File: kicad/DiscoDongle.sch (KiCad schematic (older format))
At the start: 21 parts, among them J1 USB_B, J2 RJ45, U1 FT232RL, U2 ISL81487E

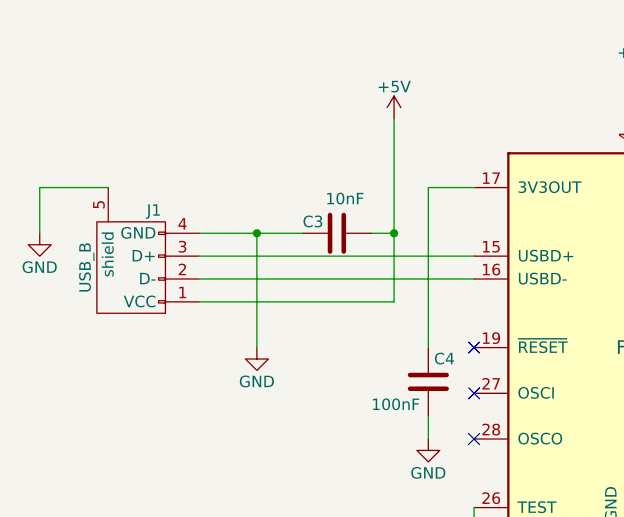
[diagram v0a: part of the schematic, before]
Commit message: Change USB to micro-B. Add part numbers
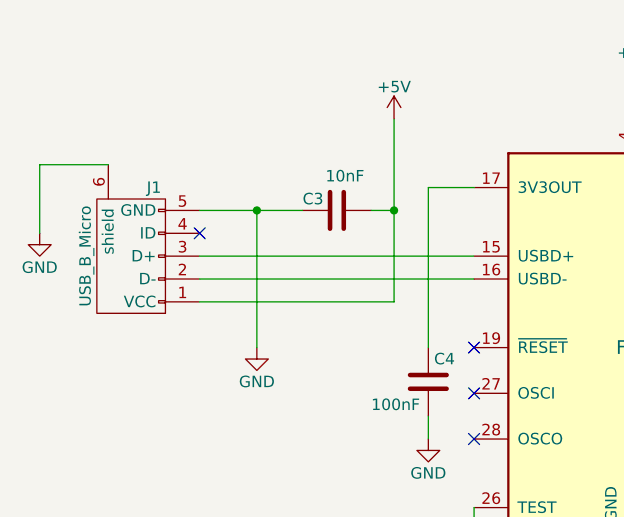
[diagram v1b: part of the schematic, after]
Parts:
- removed J1: USB_B, Connect:USB_B, symbol USB_B
- added J1: USB_B_Micro, Connect:USB_Micro-B, symbol USB_OTG
- C2: Digikey (none) -> 1276-6463-1-ND; MFN (none) -> Samsung; MPN (none) -> CL21A475KOFNNNG
- C3: Digikey (none) -> 1276-2434-1-ND; MFN (none) -> Samsung; MPN (none) -> CL21B103KAANNNC
- D1: Digikey (none) -> 475-1415-1-ND; MFN (none) -> OSRAM Opto Semiconductors Inc.; MFP (none) -> LH R974-LP-1
- D2: Digikey (none) -> 475-1415-1-ND; MFN (none) -> OSRAM; MFP (none) -> LH R974-LP-1
- D3, D4: Digikey (none) -> 475-1410-1-ND; MFN (none) -> OSRAM; MPN (none) -> LG R971-KN-1
- J2: Digikey (none) -> 609-1046-ND; MFN (none) -> Amphenol FCI; MPN (none) -> 54602-908LF
- R7: Digikey (none) -> RMCF0805JT120RCT-ND; MFN (none) -> Stackpole Electronics Inc.; MPN (none) -> RMCF0805JT120R
- U1: Digikey (none) -> 768-1007-1-ND; MFN (none) -> FTDI; MPN (none) -> FT232RL
- U2: Digikey (none) -> ISL81487EIBZ-TCT-ND; MFN (none) -> Intersil; MFP (none) -> ISL81487EIBZ-T
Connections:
- net +5V: now also J1.1 (VCC)
- net GND: now also J1.5 (GND), J1.6 (shield)
- net at U1.15 (USBD+): now also J1.3 (D+)
- net at U1.16 (USBD-): now also J1.2 (D-)
- no-connect marks 12 -> 13
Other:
- moved on the sheet: C3
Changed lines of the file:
@@
 F 2 "Housings_SSOP:SSOP-28_5.3x10.2mm_Pitch0.65mm" H 3750 2300 60  0001 C CNN
 F 3 "" H 3750 2300 60  0000 C CNN
+F 4 "FTDI" H 3550 2350 60  0001 C CNN "MFN"
+F 5 "FT232RL" H 3550 2350 60  0001 C CNN "MPN"
+F 6 "768-1007-1-ND" H 3550 2350 60  0001 C CNN "Digikey"
 	1    3550 2350
 	1    0    0    -1
-$EndComp
-$Comp
-L USB_B J1
-U 1 1 57468D47
-P 1250 1950
-F 0 "J1" V 1450 1850 50  0000 C CNN
-F 1 "USB_B" H 1200 2150 50  0000 C CNN
-F 2 "Connect:USB_B" V 1200 1850 50  0001 C CNN
-F 3 "" V 1200 1850 50  0000 C CNN
-	1    1250 1950
-	0    -1   -1   0
 $EndComp
 $Comp
@@
 F 2 "Housings_SOIC:SOIC-8_3.9x4.9mm_Pitch1.27mm" H 5800 2600 60  0001 C CNN
 F 3 "" H 5800 2600 60  0000 C CNN
+F 4 "Intersil" H 5800 2600 60  0001 C CNN "MFN"
+F 5 "ISL81487EIBZ-T" H 5800 2600 60  0001 C CNN "MFP"
+F 6 "ISL81487EIBZ-TCT-ND" H 5800 2600 60  0001 C CNN "Digikey"
 	1    5800 2600
 	1    0    0    -1
@@
 F 2 "Connect:RJ45_8" H 7350 2050 50  0001 C CNN
 F 3 "" H 7350 2050 50  0000 C CNN
+F 4 "Amphenol FCI" H 7350 2050 60  0001 C CNN "MFN"
+F 5 "54602-908LF" H 7350 2050 60  0001 C CNN "MPN"
+F 6 "609-1046-ND" H 7350 2050 60  0001 C CNN "Digikey"
 	1    7350 2050
 	0    1    -1   0
@@
 F 2 "LEDs:LED_0805" H 2900 4350 50  0001 C CNN
 F 3 "" H 2900 4350 50  0000 C CNN
+F 4 "OSRAM Opto Semiconductors Inc." H 2900 4350 60  0001 C CNN "MFN"
+F 5 "LH R974-LP-1" H 2900 4350 60  0001 C CNN "MFP"
+F 6 "475-1415-1-ND" H 2900 4350 60  0001 C CNN "Digikey"
 	1    2900 4350
 	1    0    0    -1
@@
 F 2 "LEDs:LED_0805" H 2900 4700 50  0001 C CNN
 F 3 "" H 2900 4700 50  0000 C CNN
+F 4 "OSRAM" H 2900 4700 60  0001 C CNN "MFN"
+F 5 "LH R974-LP-1" H 2900 4700 60  0001 C CNN "MFP"
+F 6 "475-1415-1-ND" H 2900 4700 60  0001 C CNN "Digikey"
 	1    2900 4700
 	1    0    0    -1
@@
 F 2 "Resistors_SMD:R_0805" V 6330 2600 50  0001 C CNN
 F 3 "" H 6400 2600 50  0000 C CNN
+F 4 "Stackpole Electronics Inc." H 6400 2600 60  0001 C CNN "MFN"
+F 5 "RMCF0805JT120R" H 6400 2600 60  0001 C CNN "MPN"
+F 6 "RMCF0805JT120RCT-ND" H 6400 2600 60  0001 C CNN "Digikey"
 	1    6400 2600
 	0    1    1    0
@@
 L C C3
 U 1 1 5746D054
-P 2150 1850
-F 0 "C3" V 2100 1700 50  0000 L CNN
-F 1 "10nF" V 2000 1800 50  0000 L CNN
-F 2 "Capacitors_SMD:C_0805" H 2188 1700 50  0001 C CNN
-F 3 "" H 2150 1850 50  0000 C CNN
-	1    2150 1850
+P 2150 1750
+F 0 "C3" V 2100 1600 50  0000 L CNN
+F 1 "10nF" V 2000 1700 50  0000 L CNN
+F 2 "Capacitors_SMD:C_0805" H 2188 1600 50  0001 C CNN
+F 3 "" H 2150 1750 50  0000 C CNN
+F 4 "Samsung" H 2150 1750 60  0001 C CNN "MFN"
+F 5 "CL21B103KAANNNC" H 2150 1750 60  0001 C CNN "MPN"
+F 6 "1276-2434-1-ND" H 2150 1750 60  0001 C CNN "Digikey"
+	1    2150 1750
 	0    1    1    0
 $EndComp
@@
 F 2 "Capacitors_SMD:C_0805" H 1638 3600 50  0001 C CNN
 F 3 "" H 1600 3750 50  0000 C CNN
+F 4 "Samsung" H 1600 3750 60  0001 C CNN "MFN"
+F 5 "CL21A475KOFNNNG" H 1600 3750 60  0001 C CNN "MPN"
+F 6 "1276-6463-1-ND" H 1600 3750 60  0001 C CNN "Digikey"
 	1    1600 3750
 	1    0    0    -1
@@
 F 2 "LEDs:LED_0805" H 4500 4300 50  0001 C CNN
 F 3 "" H 4500 4300 50  0000 C CNN
+F 4 "OSRAM" H 4500 4300 60  0001 C CNN "MFN"
+F 5 "LG R971-KN-1" H 4500 4300 60  0001 C CNN "MPN"
+F 6 "475-1410-1-ND" H 4500 4300 60  0001 C CNN "Digikey"
 	1    4500 4300
 	1    0    0    -1
@@
 F 2 "LEDs:LED_0805" H 4500 4750 50  0001 C CNN
 F 3 "" H 4500 4750 50  0000 C CNN
+F 4 "OSRAM" H 4500 4750 60  0001 C CNN "MFN"
+F 5 "LG R971-KN-1" H 4500 4750 60  0001 C CNN "MPN"
+F 6 "475-1410-1-ND" H 4500 4750 60  0001 C CNN "Digikey"
 	1    4500 4750
 	1    0    0    -1
@@
 	2400 2150 1550 2150
 Wire Wire Line
-	2400 1350 2400 2150
-Connection ~ 2400 1850
-Wire Wire Line
-	2300 1850 2400 1850
-Wire Wire Line
-	1550 1850 2000 1850
-Wire Wire Line
-	1800 2350 1800 1850
-Connection ~ 1800 1850
-Wire Wire Line
-	850  1850 850  1650
-Wire Wire Line
-	850  1650 1150 1650
+	850  1550 850  1850
+$Comp
+L USB_OTG J1
+U 1 1 5809CCCE
+P 1250 1950
+F 0 "J1" V 1550 1850 50  0000 C CNN
+F 1 "USB_B_Micro" H 1250 2150 50  0000 C CNN
+F 2 "Connect:USB_Micro-B" V 1200 1850 50  0001 C CNN
+F 3 "" V 1200 1850 50  0000 C CNN
+F 4 "Amphenol FCI" V 1250 1950 60  0001 C CNN "MFN"
+F 5 "10118194-0001LF" V 1250 1950 60  0001 C CNN "MPN"
+F 6 "609-4618-1-ND" V 1250 1950 60  0001 C CNN "Digikey"
+	1    1250 1950
+	0    -1   -1   0
+$EndComp
+Wire Wire Line
+	1150 1550 850  1550
+Wire Wire Line
+	2400 2150 2400 1350
+Wire Wire Line
+	2300 1750 2400 1750
+Connection ~ 2400 1750
+Wire Wire Line
+	2000 1750 1550 1750
+Wire Wire Line
+	1800 2350 1800 1750
+Connection ~ 1800 1750
+NoConn ~ 1550 1850
 $EndSCHEMATC

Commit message: Micro USB
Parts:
- D1, D2: symbol LED -> LED-RESCUE-DiscoDongle; MFP LH R974-LP-1 -> (none); MPN (none) -> LH R974-LP-1
- D3, D4: symbol LED -> LED-RESCUE-DiscoDongle
- J1: symbol USB_OTG -> USB_OTG-RESCUE-DiscoDongle
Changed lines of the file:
@@
 $EndComp
 $Comp
-L LED D1
+L LED-RESCUE-DiscoDongle D1
 U 1 1 5746A4EF
 P 2900 4350
@@
 F 3 "" H 2900 4350 50  0000 C CNN
 F 4 "OSRAM Opto Semiconductors Inc." H 2900 4350 60  0001 C CNN "MFN"
-F 5 "LH R974-LP-1" H 2900 4350 60  0001 C CNN "MFP"
+F 5 "LH R974-LP-1" H 2900 4350 60  0001 C CNN "MPN"
 F 6 "475-1415-1-ND" H 2900 4350 60  0001 C CNN "Digikey"
 	1    2900 4350
@@
 $EndComp
 $Comp
-L LED D2
+L LED-RESCUE-DiscoDongle D2
 U 1 1 5746A53E
 P 2900 4700
@@
 F 3 "" H 2900 4700 50  0000 C CNN
 F 4 "OSRAM" H 2900 4700 60  0001 C CNN "MFN"
-F 5 "LH R974-LP-1" H 2900 4700 60  0001 C CNN "MFP"
+F 5 "LH R974-LP-1" H 2900 4700 60  0001 C CNN "MPN"
 F 6 "475-1415-1-ND" H 2900 4700 60  0001 C CNN "Digikey"
 	1    2900 4700
@@
 Daisy
 $Comp
-L LED D3
+L LED-RESCUE-DiscoDongle D3
 U 1 1 5748F519
 P 4500 4300
@@
 Signal
 $Comp
-L LED D4
+L LED-RESCUE-DiscoDongle D4
 U 1 1 57490E65
 P 4500 4750
@@
 	850  1550 850  1850
 $Comp
-L USB_OTG J1
+L USB_OTG-RESCUE-DiscoDongle J1
 U 1 1 5809CCCE
 P 1250 1950
